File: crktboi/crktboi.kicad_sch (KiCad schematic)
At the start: 0 parts

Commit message: lil pcb
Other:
- added sheet oscillator (oscillator.kicad_sch)
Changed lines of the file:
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@@
 	(generator_version "10.0")
 	(paper "A4")
+	(sheet
+		(at 46.99 87.63)
+		(size 83.82 58.42)
+		(exclude_from_sim no)
+		(in_bom yes)
+		(on_board yes)
+		(dnp no)
+		(fields_autoplaced yes)
+		(stroke
+			(width 0.1524)
+			(type solid)
+		)
+		(fill
+			(color 0 0 0 0)
+		)
+		(property "Sheetname" "oscillator"
+			(at 46.99 86.9184 0)
+			(show_name no)
+			(do_not_autoplace no)
+			(effects
+				(font
+					(size 1.27 1.27)
+				)
+				(justify left bottom)
+			)
+		)
+		(property "Sheetfile" "oscillator.kicad_sch"
+			(at 46.99 146.6346 0)
+			(show_name no)
+			(do_not_autoplace no)
+			(effects
+				(font
+					(size 1.27 1.27)
+				)
+				(justify left top)
+			)
+		)
+		(instances
+			(project "crktboi"
+				(path "/26f57786-a21e-415f-baa1-e47de8f75073"
+					(page "2")
+				)
+			)
+		)
+	)
 	(sheet_instances
 		(path "/"

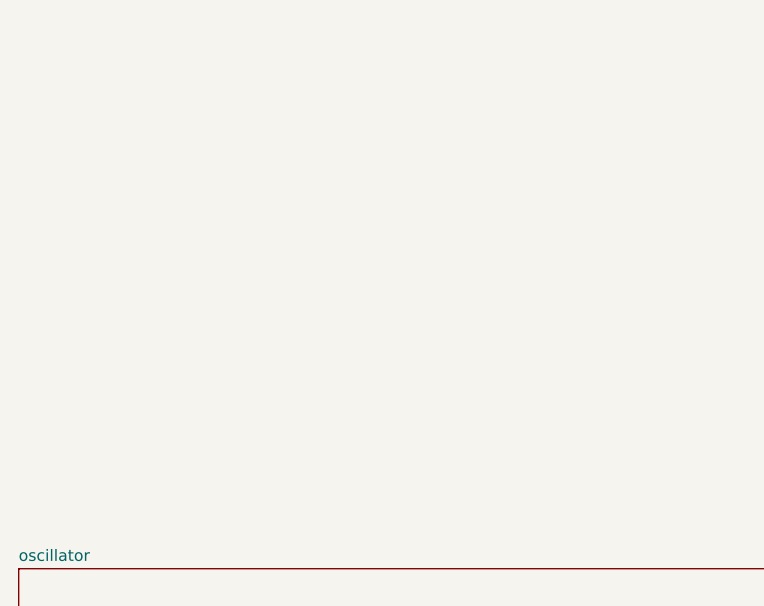
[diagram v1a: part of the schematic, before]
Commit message: Added the power circuit to the design and considered VBAT_OK as the power control output for the design. Still todo is reducing capacitor bank size and adjusting BQ25505 parameters
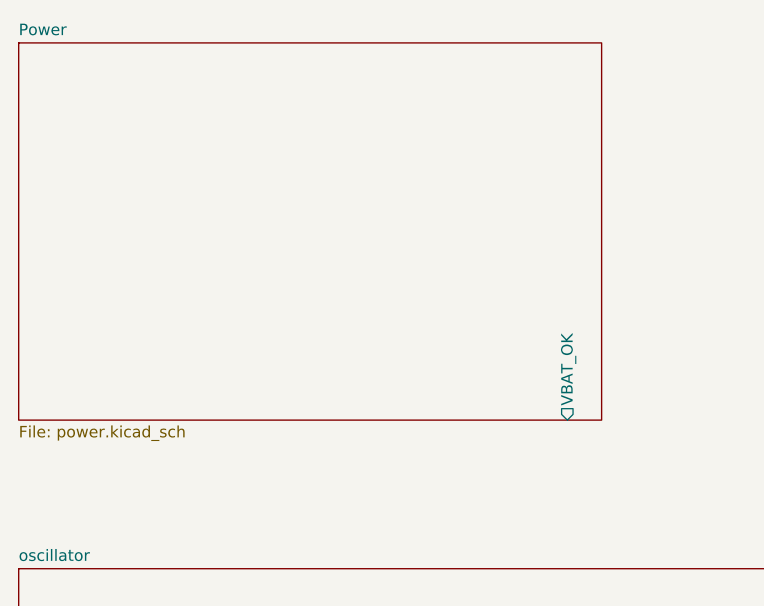
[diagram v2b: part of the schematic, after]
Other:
- added sheet Power (power.kicad_sch)
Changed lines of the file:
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@@
+		)
+	)
+	(sheet
+		(at 46.99 29.21)
+		(size 64.77 41.91)
+		(exclude_from_sim no)
+		(in_bom yes)
+		(on_board yes)
+		(dnp no)
+		(fields_autoplaced yes)
+		(stroke
+			(width 0.1524)
+			(type solid)
+		)
+		(fill
+			(color 0 0 0 0)
+		)
+		(property "Sheetname" "Power"
+			(at 46.99 28.4984 0)
+			(show_name no)
+			(do_not_autoplace no)
+			(effects
+				(font
+					(size 1.27 1.27)
+				)
+				(justify left bottom)
+			)
+		)
+		(property "Sheetfile" "power.kicad_sch"
+			(at 46.99 71.7046 0)
+			(show_name no)
+			(do_not_autoplace no)
+			(effects
+				(font
+					(size 1.27 1.27)
+				)
+				(justify left top)
+			)
+		)
+		(pin "VBAT_OK" output
+			(at 107.95 71.12 270)
+			(effects
+				(font
+					(size 1.27 1.27)
+				)
+				(justify left)
+			)
+		)
+		(instances
+			(project "crktboi"
+				(path "/26f57786-a21e-415f-baa1-e47de8f75073"
+					(page "3")
+				)
+			)
 		)
 	)

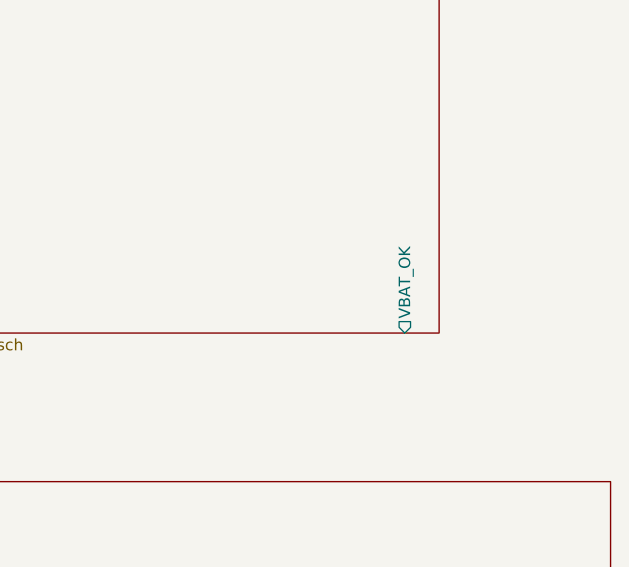
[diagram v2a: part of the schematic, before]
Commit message: Added a plan document & updated  design with tweaks for 3S3P photodiodes
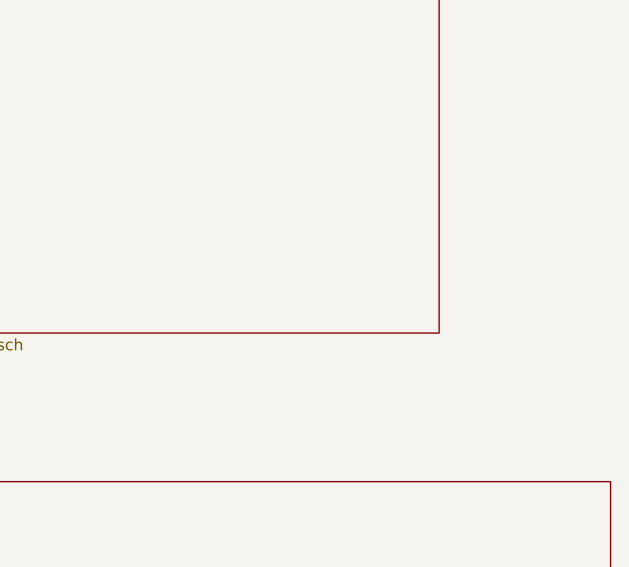
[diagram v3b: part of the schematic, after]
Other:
- sheet Power ports: added none; removed VBAT_OK
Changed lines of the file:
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@@
-			)
-		)
-		(pin "VBAT_OK" output
-			(at 107.95 71.12 270)
-			(effects
-				(font
-					(size 1.27 1.27)
-				)
-				(justify left)
 			)
 		)

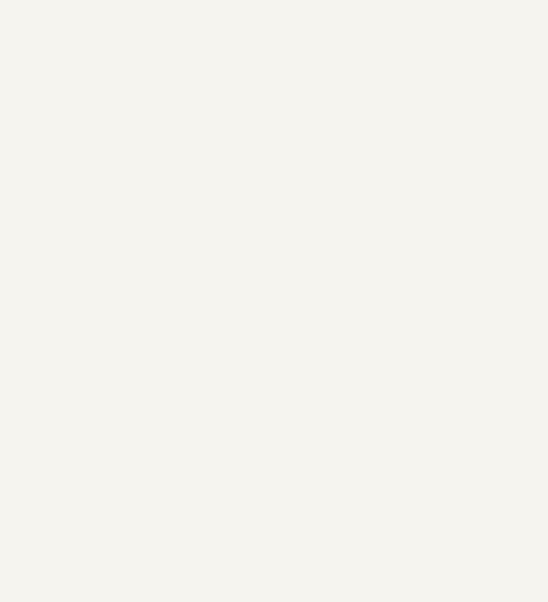
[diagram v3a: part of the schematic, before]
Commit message: Added resistors as legs for the cicada and updated LCSC part numbers for new parts
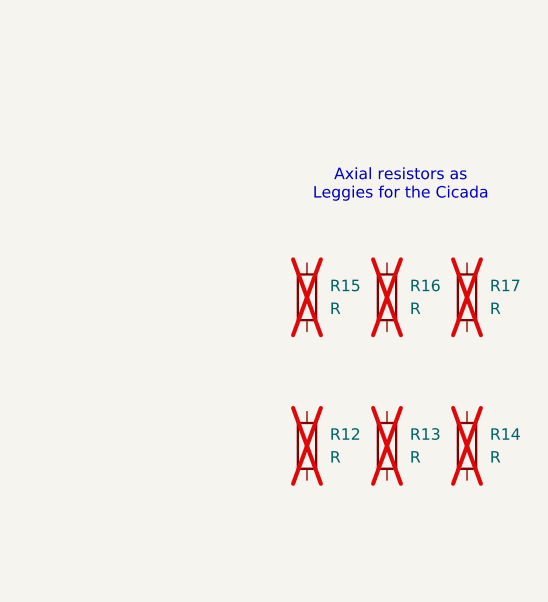
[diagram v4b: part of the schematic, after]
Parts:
- added R12, R13, R14, R15, R16, R17: R, Resistor_THT:R_Axial_DIN0204_L3.6mm_D1.6mm_P5.08mm_Horizontal, symbol Device:R
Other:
- note added: "Axial resistors as Leggies for the Cicada"
